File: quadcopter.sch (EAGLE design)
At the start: 67 parts, among them J1 AVR_SPI_PRG_6NS, U1 ATMEGA128RFA1, U2 IMU_LSM9DS1TR, Y1 16MHz

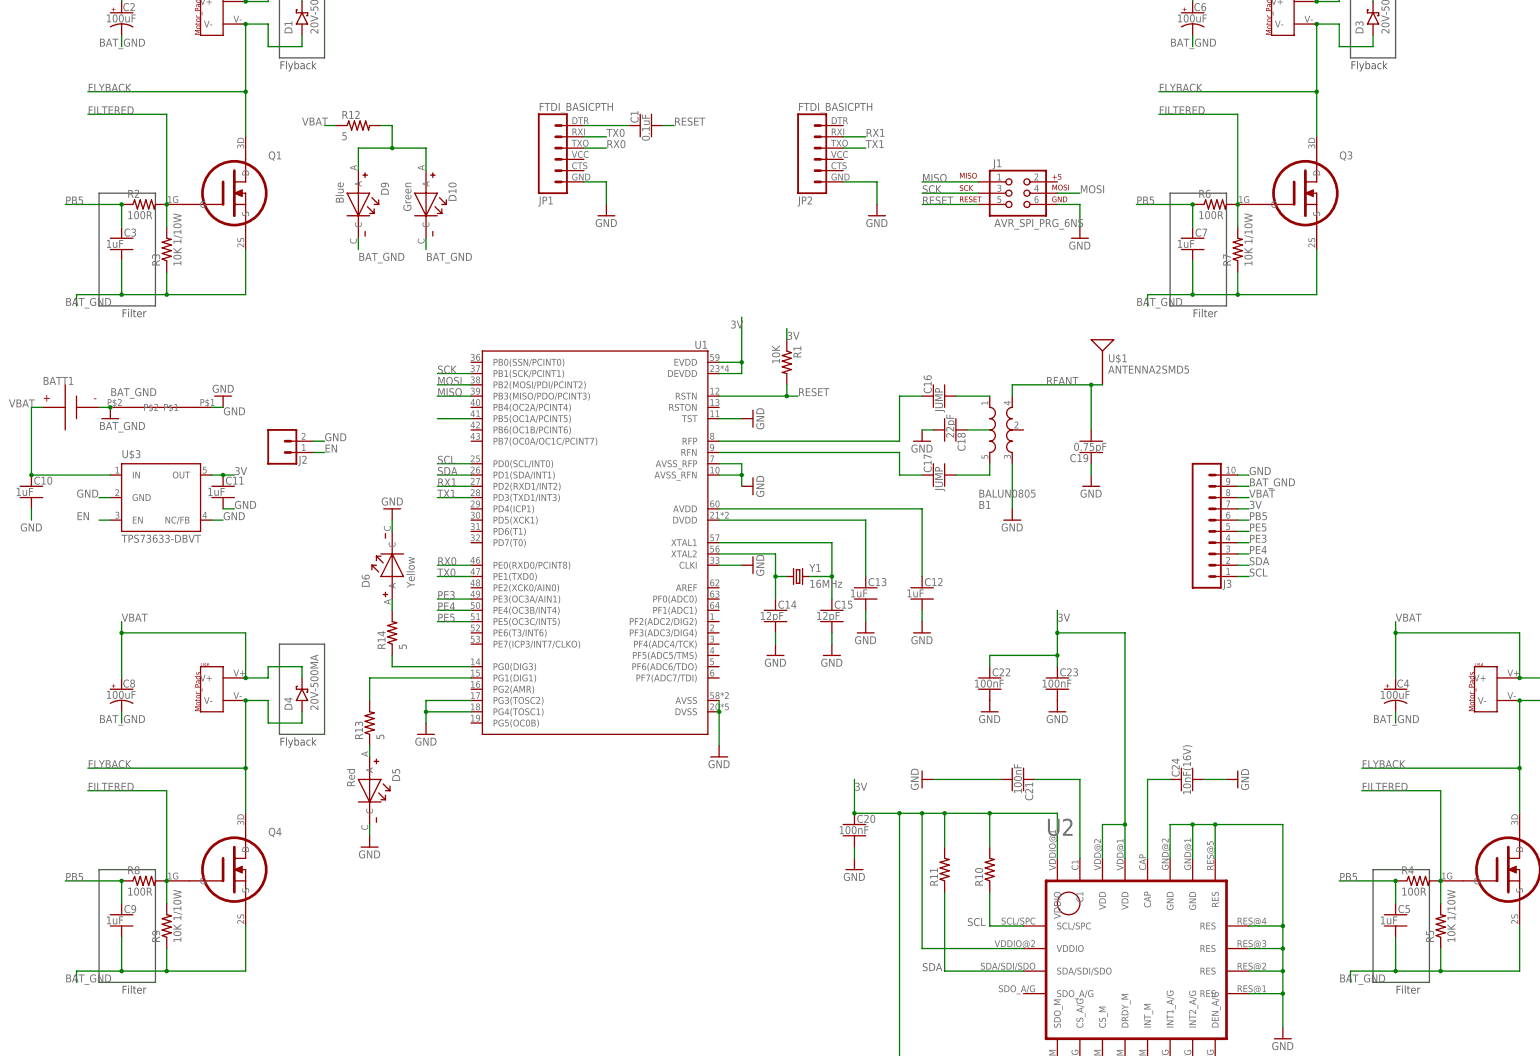
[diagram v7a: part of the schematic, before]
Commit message: changes to schematic and connie lbr
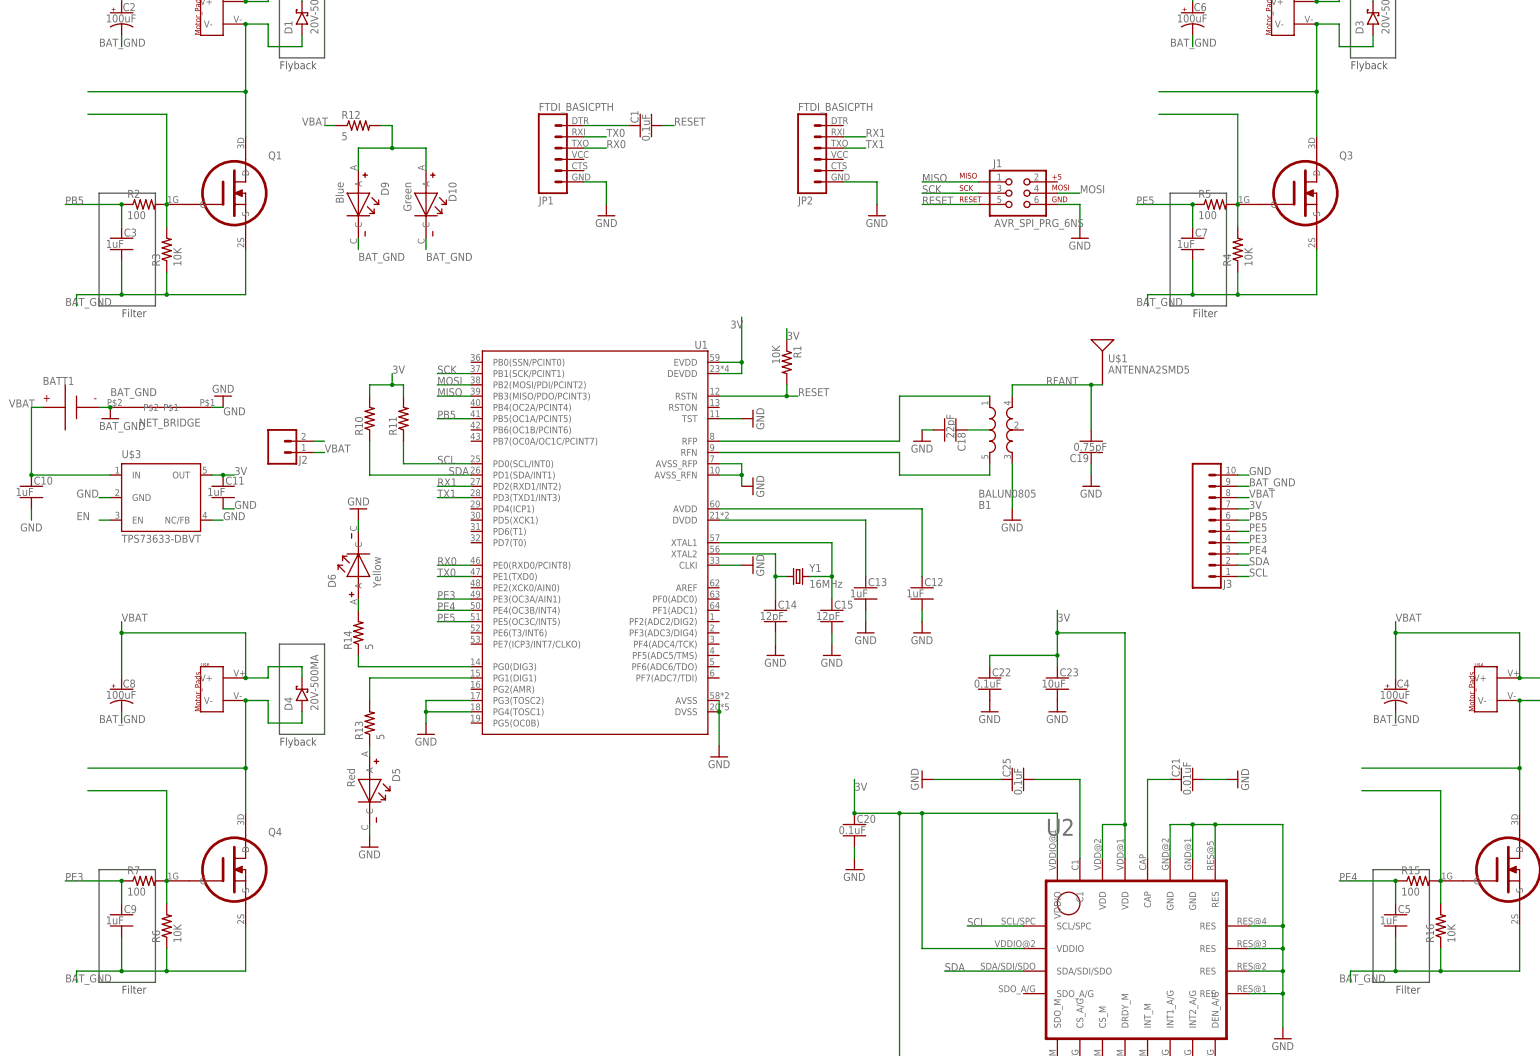
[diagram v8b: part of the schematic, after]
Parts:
- removed C16, C17: JUMP, quadparts_prebuilt:CAPACITOR-NP_SMD-2012-0805_CERAMIC
- removed C24: 10nF(16V), quadparts_prebuilt:CAPACITOR-NP_SMD-2012-0805_CERAMIC
- removed R8: 100R, quadparts_prebuilt:RESISTOR_SMD-2012-0805-100
- removed R9: 10K 1/10W, quadparts_prebuilt:RESISTOR_SMD-2012-0805-100
- added C25: 0.1uF, quadparts_prebuilt:CAPACITOR-NP_SMD-2012-0805_CERAMIC-0.1UF
- added R15: 100, quadparts_prebuilt:RESISTOR_SMD-2012-0805-100
- added R16: 10K, quadparts_prebuilt:RESISTOR_SMD-2012-0805-10K
- C20, C22: value 100nF -> 0.1uF; device quadparts_prebuilt:CAPACITOR-NP_SMD-2012-0805_CERAMIC -> quadparts_prebuilt:CAPACITOR-NP_SMD-2012-0805_CERAMIC-0.1UF
- C21: value 100nF -> 0.01uF; device quadparts_prebuilt:CAPACITOR-NP_SMD-2012-0805_CERAMIC -> quadparts_prebuilt:CAPACITOR-NP_SMD-2012-0805_CERAMIC-0.01UF
- C23: value 100nF -> 10uF; device quadparts_prebuilt:CAPACITOR-NP_SMD-2012-0805_CERAMIC -> quadparts_prebuilt:CAPACITOR-NP_SMD-2012-0805_CERAMIC-10UF
- R2: value 100R -> 100
- R3: value 10K 1/10W -> 10K; device quadparts_prebuilt:RESISTOR_SMD-2012-0805-100 -> quadparts_prebuilt:RESISTOR_SMD-2012-0805-10K
- R4, R6: value 100R -> 10K; device quadparts_prebuilt:RESISTOR_SMD-2012-0805-100 -> quadparts_prebuilt:RESISTOR_SMD-2012-0805-10K
- R5, R7: value 10K 1/10W -> 100
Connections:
- removed net N$16: U1.PB5(OC1A/PCINT5)
- removed net N$23: B1.IN, C16.2
- removed net N$24: B1.GND@5, C17.2
- net BAT_GND: now also R16.1, R4.1, R6.1; no longer R5.1, R7.1, R9.1
- net EN: no longer J2.1
- net FILTERED: now also R15.2, R16.2; no longer R8.2, R9.2
- net GND: now also C25.1; no longer C24.2
- net N$15: now also C25.2; no longer C21.1
- net N$17: now also C21.1; no longer C24.1
- net N$21: now also B1.IN; no longer C16.1
- net N$22: now also B1.GND@5; no longer C17.1
- net PB5: now also U1.PB5(OC1A/PCINT5); no longer C5.1, C7.1, C9.1, R4.1, R6.1, R8.1
- net PE3: now also C9.1, R7.1
- net PE4: now also C5.1, R15.1
- net PE5: now also C7.1, R5.1
- net SCL: now also R11.1; no longer R10.1
- net SDA: now also R10.1; no longer R11.1
- net VBAT: now also J2.1
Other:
- moved on the sheet: C21, D6, R10, R11, R14, R4, R5, R6, R7
